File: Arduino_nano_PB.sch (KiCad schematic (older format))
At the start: 42 parts, among them CON1 BARREL_JACK, P1 CONN_01X02, P7 CONN_01X04, Q1 BC547, Q2 BC547, Q3 BC547, Q4 2N3904BU, Q5 2N3904BU, Q6 2N3904BU, Q7 2N3904BU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

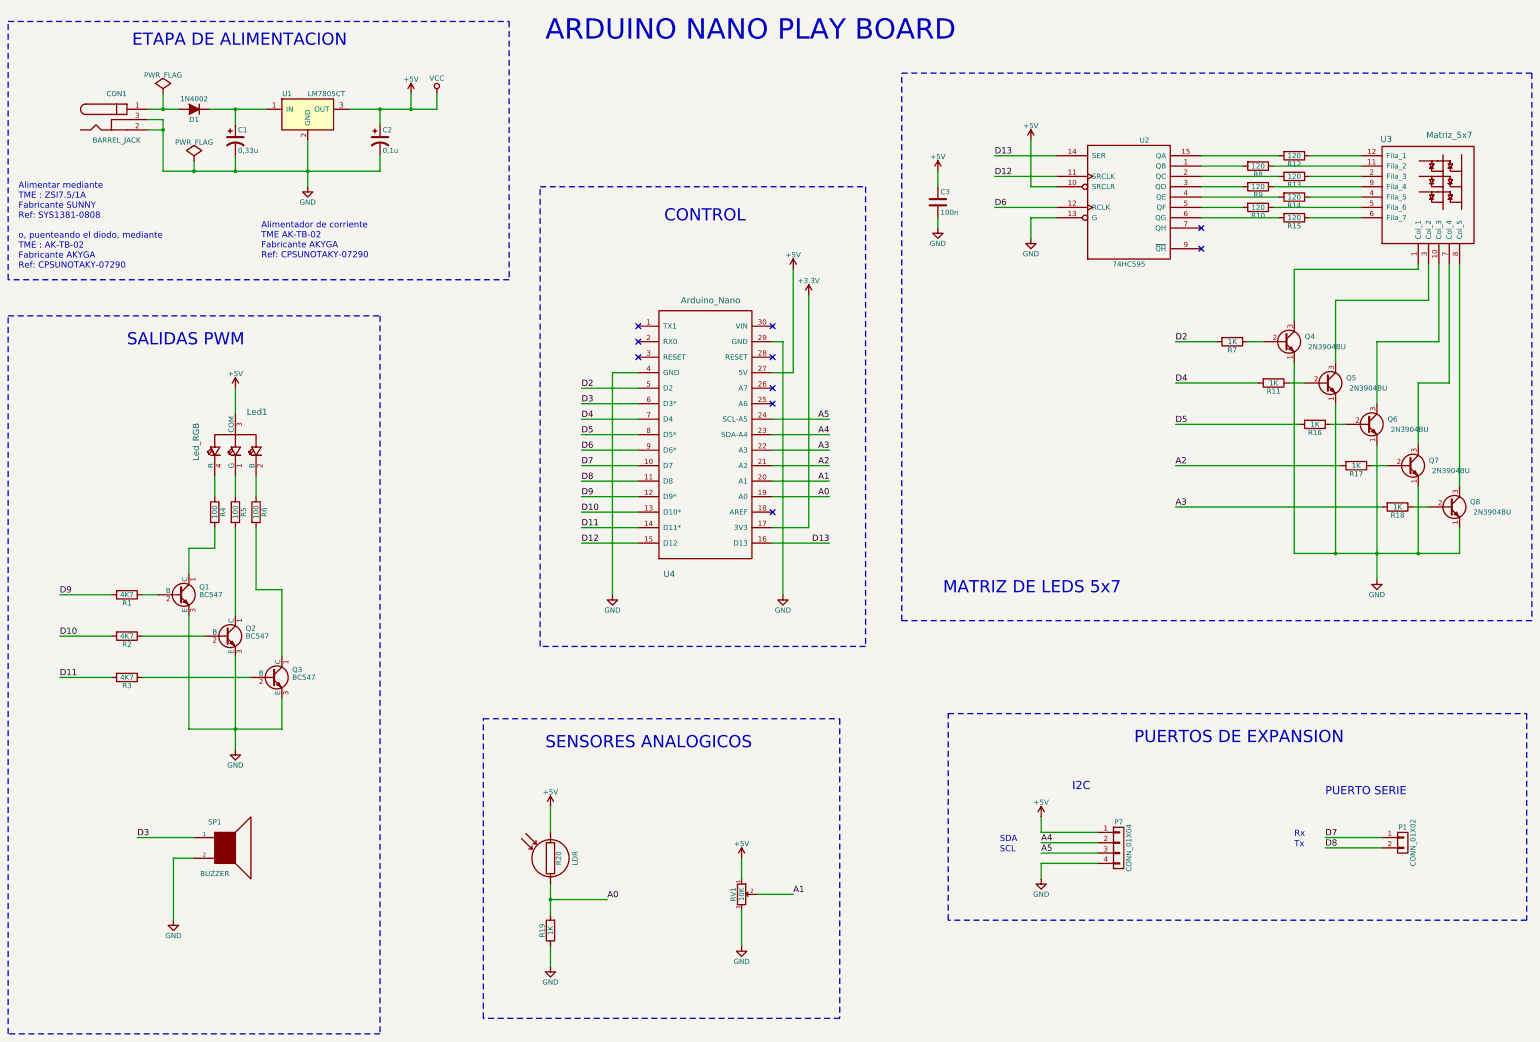
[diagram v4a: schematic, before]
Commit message: Añadidos nuevos elementos al esquema de la placa
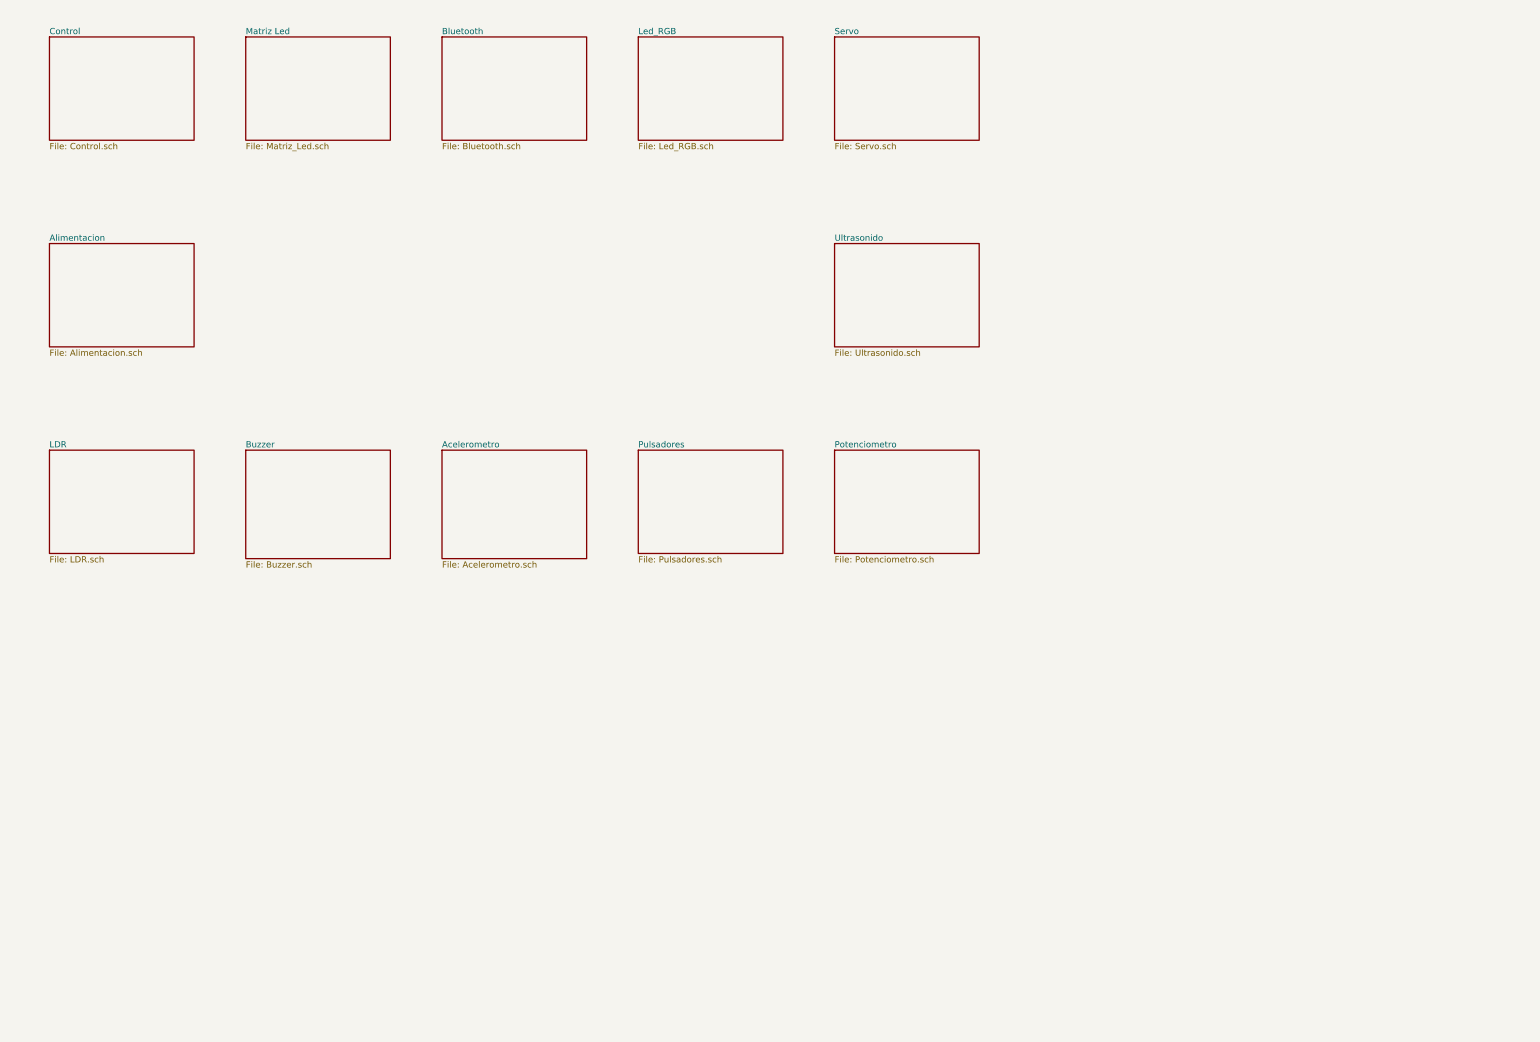
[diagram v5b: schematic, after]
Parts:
- removed C1: 0,33u, Capacitors_ThroughHole:C_Radial_D5_L11_P2, symbol CP1
- removed C2: 0,1u, Capacitors_ThroughHole:C_Radial_D5_L11_P2, symbol CP1
- removed C3: 100n, Capacitors_ThroughHole:C_Disc_D3_P2.5, symbol C
- removed CON1: BARREL_JACK, Conectores:Barrel_Jack_Hembra_CLIFF_FC68148, symbol BARREL_JACK
- removed D1: 1N4002, Diodes_ThroughHole:Diode_DO-35_SOD27_Horizontal_RM10, symbol D
- removed Led1: Led_RGB, Leds:LED_RGB_5mm_G_B_COM_R_Anodo_comun, symbol Led_RGB_Anodo_Comun
- removed P1: CONN_01X02, Pin_Headers:Pin_Header_Straight_1x02, symbol CONN_01X02
- removed P7: CONN_01X04, Pin_Headers:Pin_Header_Straight_1x04, symbol CONN_01X04
- removed Q1, Q2, Q3: BC547, Transistors:TO-92_EnLinea_Estrecho_Oval, symbol BC547
- removed Q4, Q5, Q6, Q7, Q8: 2N3904BU, Transistors:TO-92_EnLinea_Estrecho_Oval, symbol Q_NPN_EBC
- removed R1, R2, R3: 4K7, Resistencias:Resistencia_1_4_W_10_mm, symbol R
- removed R10, R12, R13, R14, R15, R8, R9: 120, Resistencias:Resistencia_1_4_W_10_mm, symbol R
- removed R11, R16, R17, R18, R19, R7: 1K, Resistencias:Resistencia_1_4_W_10_mm, symbol R
- removed R20: LDR, Sensores:LDR_TOKEN_PGM5_Series, symbol Photores
- removed R4, R5, R6: 100, Resistencias:Resistencia_1_4_W_10_mm, symbol R
- removed RV1: 10K, Potenciometros:POT_SR_PASIVES_R9011, symbol POT
- removed SP1: BUZZER, Buzzer:LOUDITY_LD-BZPN-1705, symbol SPEAKER
- removed U1: LM7805CT, TO_SOT_Packages_THT:TO-220_Neutral123_Vertical_LargePads, symbol LM7805CT
- removed U2: 74HC595, Housings_SOIC:SOIC-16_3.9x9.9mm_Pitch1.27mm, symbol 74HC595
- removed U3: Matriz_5x7, Leds:Matriz_Led_7X5, symbol Matriz_5x7_Anodo_Filas
- removed U4: Arduino_Nano, Arduino:Arduino_Nano, symbol Arduino_Nano
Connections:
- no-connect marks 10 -> 0
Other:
- note removed: "ARDUINO NANO PLAY BOARD"
- note removed: "Alimentador de corriente\nTME AK-TB-02\nFabricante AKYGA\nRef: CPSUNOTAKY-07290"
- note removed: "Alimentar mediante\nTME : ZSI7.5/1A\nFabricante SUNNY\nRef: SYS1381-0808\n\no, puenteando el diodo, mediante\nTME : AK-TB-02\nFabricante AKYGA\nRef: CPSUNOTAKY-07290"
- note removed: "CONTROL"
- note removed: "ETAPA DE ALIMENTACION"
- note removed: "I2C"
- note removed: "MATRIZ DE LEDS 5x7"
- note removed: "PUERTO SERIE"
- note removed: "PUERTOS DE EXPANSION"
- note removed: "Rx"
- note removed: "SALIDAS PWM"
- note removed: "SCL"
- note removed: "SDA"
- note removed: "SENSORES ANALOGICOS"
- note removed: "Tx"

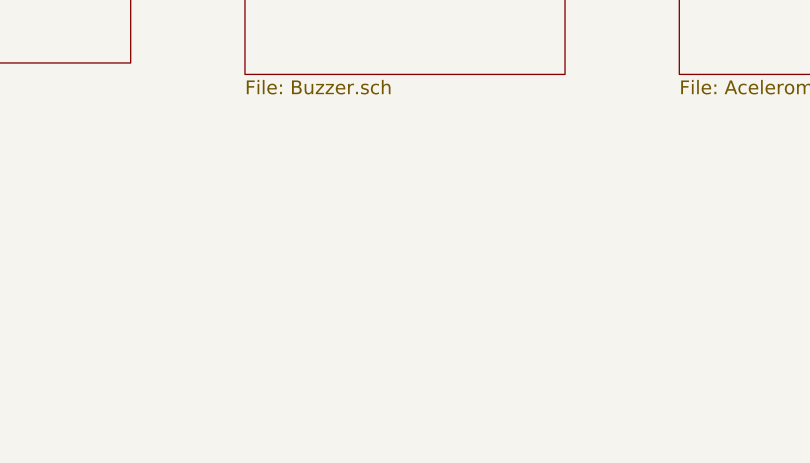
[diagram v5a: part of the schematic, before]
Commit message: añaadido zocalo para sensor de temperatura y primera distribucion sobre la PCB
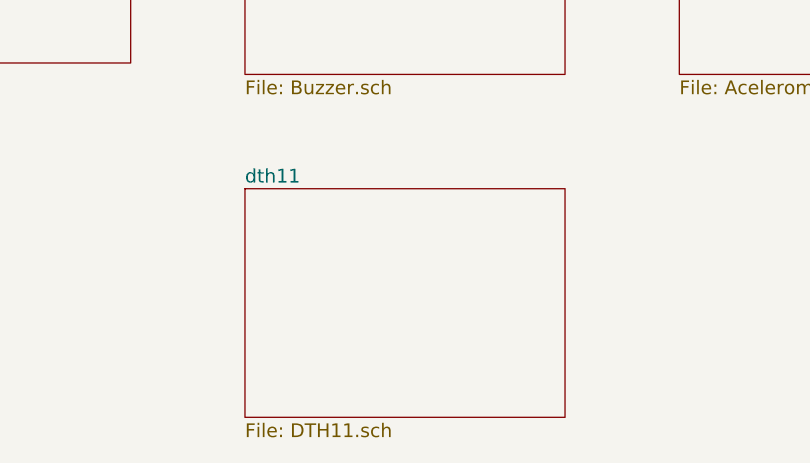
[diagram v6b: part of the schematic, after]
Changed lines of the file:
@@
 $Descr A4 11693 8268
 encoding utf-8
-Sheet 1 13
+Sheet 1 14
 Title ""
 Date "2016-07-18"
@@
 F1 "Acelerometro.sch" 60
 $EndSheet
+$Sheet
+S 3100 6500 1400 1000
+U 57993DAA
+F0 "dth11" 60
+F1 "DTH11.sch" 60
+$EndSheet
 $EndSCHEMATC

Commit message: finalizado enrutado provisional
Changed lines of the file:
@@
 $Descr A4 11693 8268
 encoding utf-8
-Sheet 1 14
+Sheet 1 15
 Title ""
 Date "2016-07-18"
@@
 $EndDescr
 $Sheet
-S 3100 950  1400 1000
-U 57939A23
-F0 "Matriz Led" 60
-F1 "Matriz_Led.sch" 60
-$EndSheet
-$Sheet
 S 1200 2950 1400 1000
 U 5793C398
@@
 F1 "DTH11.sch" 60
 $EndSheet
+$Sheet
+S 1200 6500 1400 1000
+U 579DE89E
+F0 "Encoder" 100
+F1 "Encoder.sch" 100
+$EndSheet
+$Sheet
+S 3100 950  1400 1000
+U 57939A23
+F0 "Matriz Led" 60
+F1 "Matriz_Led.sch" 60
+$EndSheet
 $EndSCHEMATC
